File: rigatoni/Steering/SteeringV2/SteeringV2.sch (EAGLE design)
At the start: 19 parts, among them J3 PCB_SCREW_TERM_3, J4 PCB_SCREW_TERM_3, J5 PCB_SCREW_TERM_8, J6 PCB_SCREW_TERM_8, J7 PCB_SCREW_TERM_3, Q1 STT4P3LLH6, U1 SN74ALVC164245DGGR, U2 NUCLEO-H743ZI-HEADER, U3 TPSM84205EAB

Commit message: Commit Internal Design Review
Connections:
- removed net N$7: D2.A, F2.2
- net +5V: now also U2G$3.+5V_CN8; no longer D2.C
- net N$1: now also Q1.D; no longer D1.A, F1.2
- net N$6: now also F1.2; no longer D1.C, Q1.D
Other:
- moved on the sheet: D1, D2
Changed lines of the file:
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@@
 <part name="SUPPLY27" library="RoboJackets-Supplies" deviceset="+3.3V" device=""/>
 <part name="SUPPLY28" library="RoboJackets-Supplies" deviceset="+5V" device=""/>
+<part name="SUPPLY25" library="RoboJackets-Supplies" deviceset="+5V" device=""/>
 </parts>
 <sheets>
@@
 <attribute name="VALUE" x="-29.464" y="84.709" size="1.778" layer="96"/>
 </instance>
-<instance part="D1" gate="G$1" x="-124.46" y="93.98" smashed="yes" rot="R90">
-<attribute name="NAME" x="-119.888" y="90.551" size="1.778" layer="95" font="vector" rot="R180"/>
-<attribute name="VALUE" x="-119.888" y="95.885" size="1.778" layer="96" font="vector" rot="R180" align="top-left"/>
-</instance>
-<instance part="D2" gate="G$1" x="0" y="93.98" smashed="yes" rot="R90">
-<attribute name="NAME" x="4.572" y="90.551" size="1.778" layer="95" font="vector" rot="R180"/>
-<attribute name="VALUE" x="4.572" y="95.885" size="1.778" layer="96" font="vector" rot="R180" align="top-left"/>
+<instance part="D1" gate="G$1" x="-124.46" y="88.9" smashed="yes">
+<attribute name="NAME" x="-127.889" y="84.328" size="1.778" layer="95" font="vector" rot="R90"/>
+<attribute name="VALUE" x="-122.555" y="84.328" size="1.778" layer="96" font="vector" rot="R90" align="top-left"/>
+</instance>
+<instance part="D2" gate="G$1" x="0" y="88.9" smashed="yes">
+<attribute name="NAME" x="-3.429" y="84.328" size="1.778" layer="95" font="vector" rot="R90"/>
+<attribute name="VALUE" x="1.905" y="84.328" size="1.778" layer="96" font="vector" rot="R90" align="top-left"/>
 </instance>
 <instance part="SUPPLY20" gate="P" x="81.28" y="15.24" smashed="yes" rot="R270">
@@
 <instance part="SUPPLY28" gate="G$1" x="106.68" y="129.54" smashed="yes" rot="R270">
 <attribute name="VALUE" x="109.855" y="131.445" size="1.778" layer="96" rot="R270"/>
+</instance>
+<instance part="SUPPLY25" gate="G$1" x="81.28" y="20.32" smashed="yes" rot="R270">
+<attribute name="VALUE" x="84.455" y="22.225" size="1.778" layer="96"/>
 </instance>
 </instances>
@@
 </segment>
 </net>
-<net name="N$1" class="0">
-<segment>
-<pinref part="F1" gate="G$1" pin="2"/>
-<pinref part="D1" gate="G$1" pin="A"/>
-<wire x1="-132.08" y1="93.98" x2="-127" y2="93.98" width="0.1524" layer="91"/>
-</segment>
-</net>
 <net name="N$2" class="0">
 <segment>
@@
 <pinref part="C1" gate="G$1" pin="1"/>
 <wire x1="10.16" y1="93.98" x2="10.16" y2="91.44" width="0.1524" layer="91"/>
-<pinref part="D2" gate="G$1" pin="C"/>
 <wire x1="5.08" y1="93.98" x2="10.16" y2="93.98" width="0.1524" layer="91"/>
 <junction x="10.16" y="93.98"/>
@@
 <junction x="104.14" y="129.54"/>
 </segment>
+<segment>
+<pinref part="U2" gate="G$3" pin="+5V_CN8"/>
+<pinref part="SUPPLY25" gate="G$1" pin="+5V"/>
+<wire x1="63.5" y1="20.32" x2="78.74" y2="20.32" width="0.1524" layer="91"/>
+</segment>
 </net>
 <net name="N$4" class="0">
@@
 <wire x1="-161.29" y1="93.98" x2="-161.29" y2="95.25" width="0.1524" layer="91"/>
 <pinref part="F1" gate="G$1" pin="1"/>
-</segment>
-</net>
-<net name="N$5" class="0">
-<segment>
-<wire x1="-30.48" y1="88.9" x2="-35.56" y2="88.9" width="0.1524" layer="91"/>
-</segment>
-</net>
-<net name="N$6" class="0">
-<segment>
-<pinref part="D1" gate="G$1" pin="C"/>
-<pinref part="Q1" gate="A" pin="D"/>
-<wire x1="-119.38" y1="93.98" x2="-111.76" y2="93.98" width="0.1524" layer="91"/>
-</segment>
-</net>
-<net name="N$7" class="0">
-<segment>
-<pinref part="F2" gate="G$1" pin="2"/>
-<pinref part="D2" gate="G$1" pin="A"/>
-<wire x1="-5.08" y1="93.98" x2="-2.54" y2="93.98" width="0.1524" layer="91"/>
 </segment>
 </net>
@@
 </segment>
 </net>
+<net name="N$1" class="0">
+<segment>
+<pinref part="Q1" gate="A" pin="D"/>
+<wire x1="-116.84" y1="93.98" x2="-111.76" y2="93.98" width="0.1524" layer="91"/>
+</segment>
+</net>
+<net name="N$6" class="0">
+<segment>
+<pinref part="F1" gate="G$1" pin="2"/>
+<wire x1="-132.08" y1="93.98" x2="-127" y2="93.98" width="0.1524" layer="91"/>
+</segment>
+</net>

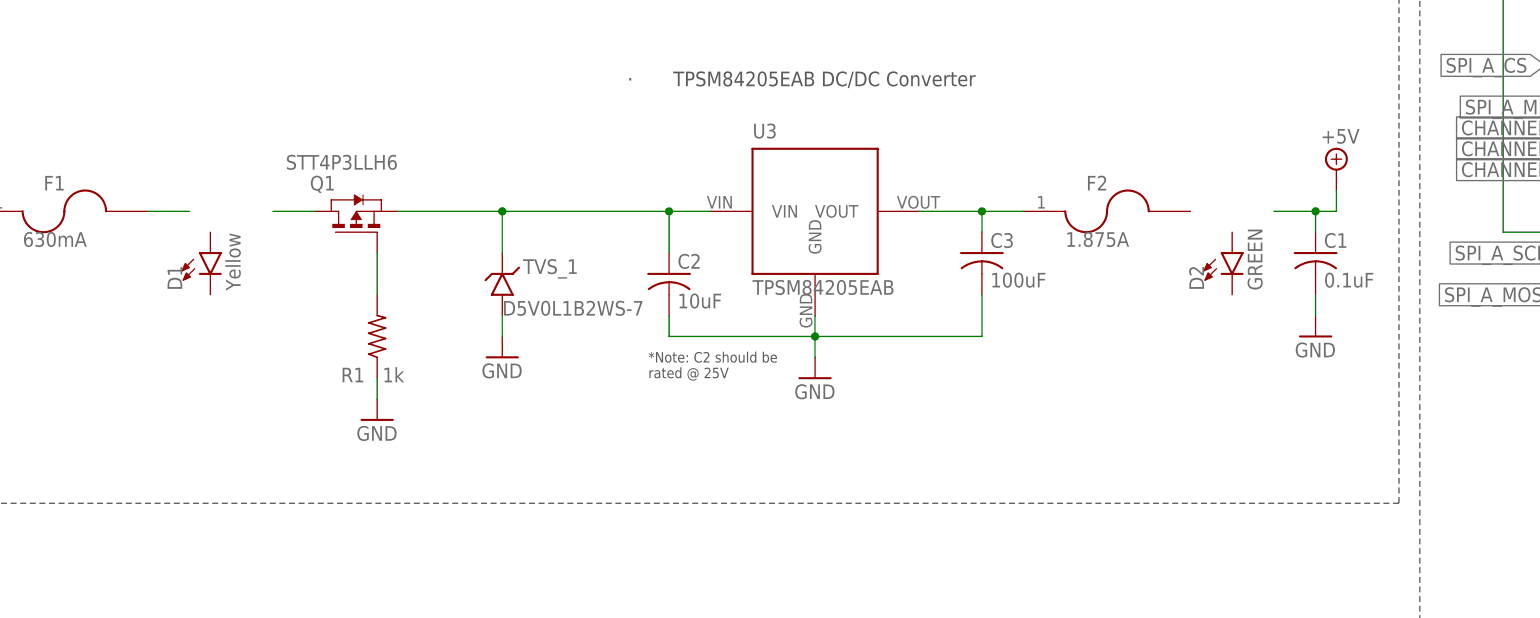
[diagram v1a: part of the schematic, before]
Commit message: Updated Common Power Circuitry
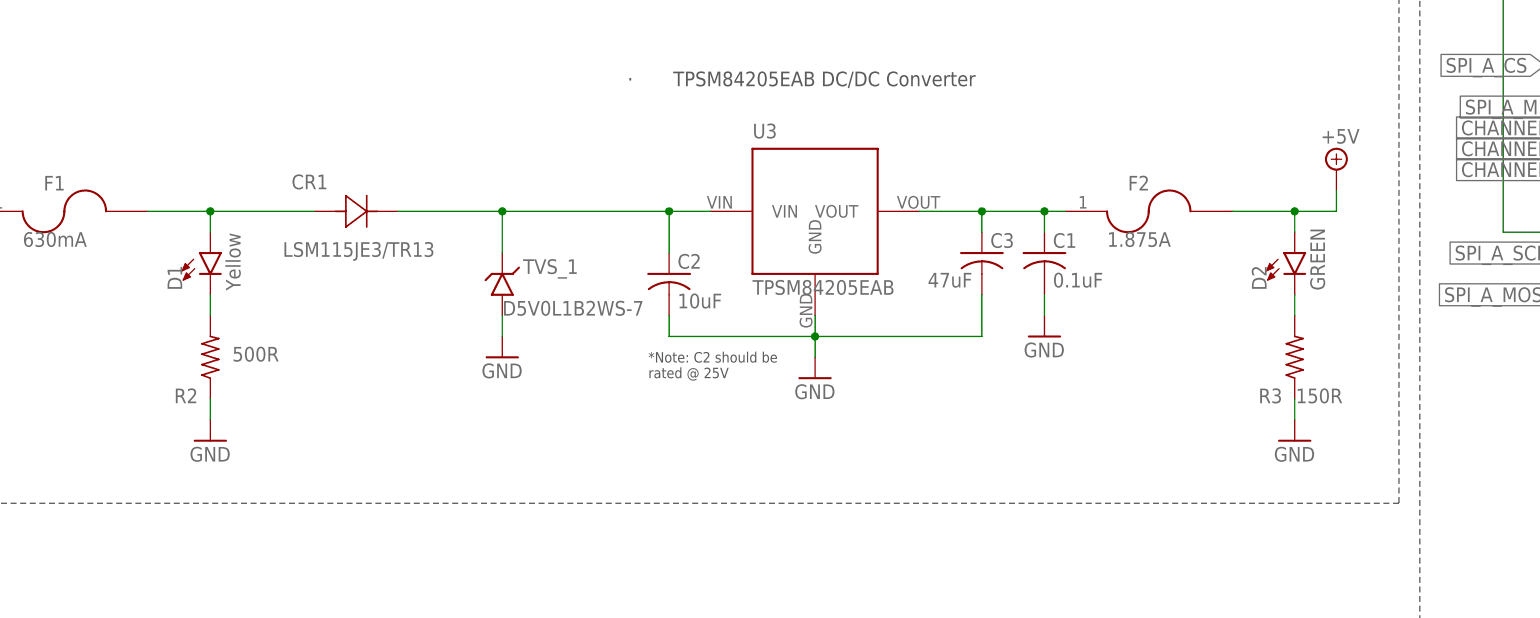
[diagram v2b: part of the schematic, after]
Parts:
- removed Q1: STT4P3LLH6, RoboJackets-Discrete:STT4P3LLH6
- removed R1: 1k, rcl:R-US_R0603
- added CR1: LSM115JE3/TR13, RoboRacing_STM:LSM115JE3/TR13
- added R2: 500R, rcl:R-US_R0603
- added R3: 150R, rcl:R-US_R0603
- C3: value 100uF -> 47uF
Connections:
- removed net N$2: Q1.G, R1.2
- new net N$5: D1.C, R2.2
- net +5V: now also D2.A, F2.2; no longer C1.1
- net 5V_MAIN: now also C1.1
- net GND: now also R2.1, R3.1; no longer R1.1
- net N$1: now also CR1.2, D1.A, F1.2; no longer Q1.D
- net N$3: now also CR1.1; no longer Q1.S
- net N$6: now also D2.C, R3.2; no longer F1.2
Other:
- moved on the sheet: C1, D2, F2

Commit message: Steering Schematic Updated After Internal Design Review
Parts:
- removed J5, J6: PCB_SCREW_TERM_8, RoboJackets-Connectors:PCB_SCREW_TERM_8
- added J2: B10B-XH-A(LF)(SN), RoboRacing_STM:B10B-XH-A(LF)(SN)
- R3: value 150R -> 147R
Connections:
- new net CHANNEL_A_ENC: J2.8, U1.1B5
- new net CHANNEL_B_ENC: J2.7, U1.1B3
- new net CHANNEL_Z_ENC: J2.9, U1.1B7
- new net SPI_A_CS_ENC: J2.1, U1.2B3
- net +5V: now also J2.5; no longer J5.6
- net CHANNEL_A: no longer J6.2, U1.1B5
- net CHANNEL_B: no longer J5.8, U1.1B3
- net CHANNEL_Z: no longer J6.4, U1.1B7
- net GND: now also J2.3, U1.1A1, U1.1A4, U1.1A6, U1.1A8, U1.1B1, U1.1B4, U1.1B6, U1.1B8, U1.2A4, U1.2A5, U1.2A6, U1.2A7, U1.2A8, U1.2B4, U1.2B5, U1.2B6, U1.2B7, U1.2B8; no longer J5.4
- net SPI_A_CS: now also U1.2A3; no longer J5.2, U1.1A1, U1.1B1
- net SPI_A_MISO: now also J2.2; no longer J5.3
- net SPI_A_MOSI: now also J2.6; no longer J5.7
- net SPI_A_SCK: now also J2.4; no longer J5.5

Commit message: Finished Steering V2 Board Layout
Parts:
- removed C1: 0.1uF, rcl:C-US025-024X044
- removed C2: 10uF, rcl:C-US025-024X044
- removed C3: 47uF, rcl:C-US025-024X044
- added C4: 0.1uF, rcl:C-USC0805
- added C5: 47uF, rcl:C-USC0805
- added C6: 10uF, rcl:C-USC0805
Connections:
- net 5V_MAIN: now also C4.1, C5.1; no longer C1.1, C3.1
- net GND: now also C4.2, C5.2, C6.2; no longer C1.2, C2.2, C3.2
- net N$3: now also C6.1; no longer C2.1
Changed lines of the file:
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@@
 <part name="U3" library="RoboRacing_STM" deviceset="TPSM84205EAB" device=""/>
 <part name="SUPPLY6" library="RoboJackets-Supplies" deviceset="GND" device=""/>
-<part name="C2" library="rcl" library_urn="urn:adsk.eagle:library:334" deviceset="C-US" device="025-024X044" package3d_urn="urn:adsk.eagle:package:23630/1" value="10uF"/>
 <part name="F2" library="RoboJackets-Fuses" deviceset="SMD_FUSE" device="0603" value="1.875A"/>
 <part name="SUPPLY9" library="RoboJackets-Supplies" deviceset="GND" device=""/>
@@
 <part name="SUPPLY1" library="RoboJackets-Supplies" deviceset="+5V" device=""/>
 <part name="SUPPLY19" library="RoboJackets-Supplies" deviceset="+5V" device=""/>
-<part name="C1" library="rcl" library_urn="urn:adsk.eagle:library:334" deviceset="C-US" device="025-024X044" package3d_urn="urn:adsk.eagle:package:23630/1" value="0.1uF"/>
 <part name="SUPPLY3" library="RoboJackets-Supplies" deviceset="GND" device=""/>
-<part name="C3" library="rcl" library_urn="urn:adsk.eagle:library:334" deviceset="C-US" device="025-024X044" package3d_urn="urn:adsk.eagle:package:23630/1" value="47uF"/>
 <part name="D1" library="RoboJackets-LEDs" deviceset="LED-YELLOW" device="0603" value="Yellow"/>
 <part name="D2" library="RoboJackets-LEDs" deviceset="LED-GREEN" device="1206" value="GREEN"/>
@@
 <part name="SUPPLY34" library="RoboJackets-Supplies" deviceset="GND" device=""/>
 <part name="SUPPLY35" library="RoboJackets-Supplies" deviceset="GND" device=""/>
+<part name="C4" library="rcl" library_urn="urn:adsk.eagle:library:334" deviceset="C-US" device="C0805" package3d_urn="urn:adsk.eagle:package:23617/2" value="0.1uF"/>
+<part name="C5" library="rcl" library_urn="urn:adsk.eagle:library:334" deviceset="C-US" device="C0805" package3d_urn="urn:adsk.eagle:package:23617/2" value="47uF"/>
+<part name="C6" library="rcl" library_urn="urn:adsk.eagle:library:334" deviceset="C-US" device="C0805" package3d_urn="urn:adsk.eagle:package:23617/2" value="10uF"/>
 </parts>
 <sheets>
@@
 <attribute name="VALUE" x="-53.34" y="71.12" size="1.778" layer="96"/>
 </instance>
-<instance part="C2" gate="G$1" x="-68.58" y="86.36" smashed="yes">
-<attribute name="NAME" x="-67.564" y="86.995" size="1.778" layer="95"/>
-<attribute name="VALUE" x="-67.564" y="82.169" size="1.778" layer="96"/>
-</instance>
 <instance part="F2" gate="G$1" x="-10.16" y="93.98" smashed="yes">
 <attribute name="NAME" x="-12.7" y="96.52" size="1.778" layer="95"/>
@@
 <attribute name="VALUE" x="-24.765" y="31.115" size="1.778" layer="96"/>
 </instance>
-<instance part="C1" gate="G$1" x="-22.86" y="88.9" smashed="yes">
-<attribute name="NAME" x="-21.844" y="89.535" size="1.778" layer="95"/>
-<attribute name="VALUE" x="-21.844" y="84.709" size="1.778" layer="96"/>
-</instance>
 <instance part="SUPPLY3" gate="G$1" x="-22.86" y="78.74" smashed="yes">
 <attribute name="VALUE" x="-25.4" y="76.2" size="1.778" layer="96"/>
-</instance>
-<instance part="C3" gate="G$1" x="-30.48" y="88.9" smashed="yes">
-<attribute name="NAME" x="-29.464" y="89.535" size="1.778" layer="95"/>
-<attribute name="VALUE" x="-37.084" y="84.709" size="1.778" layer="96"/>
 </instance>
 <instance part="D1" gate="G$1" x="-124.46" y="88.9" smashed="yes">
@@
 <instance part="SUPPLY35" gate="G$1" x="104.14" y="96.52" smashed="yes" rot="R90">
 <attribute name="VALUE" x="109.22" y="96.52" size="1.016" layer="96" rot="R180"/>
+</instance>
+<instance part="C4" gate="G$1" x="-22.86" y="88.9" smashed="yes">
+<attribute name="NAME" x="-21.844" y="89.535" size="1.778" layer="95"/>
+<attribute name="VALUE" x="-21.844" y="84.709" size="1.778" layer="96"/>
+</instance>
+<instance part="C5" gate="G$1" x="-30.48" y="88.9" smashed="yes">
+<attribute name="NAME" x="-29.464" y="89.535" size="1.778" layer="95"/>
+<attribute name="VALUE" x="-29.464" y="84.709" size="1.778" layer="96"/>
+</instance>
+<instance part="C6" gate="G$1" x="-68.58" y="86.36" smashed="yes">
+<attribute name="NAME" x="-67.564" y="86.995" size="1.778" layer="95"/>
+<attribute name="VALUE" x="-67.564" y="82.169" size="1.778" layer="96"/>
 </instance>
 </instances>
@@
 <pinref part="SUPPLY6" gate="G$1" pin="GND"/>
 <wire x1="-50.8" y1="81.28" x2="-50.8" y2="78.74" width="0.1524" layer="91"/>
-<pinref part="C2" gate="G$1" pin="2"/>
 <wire x1="-50.8" y1="78.74" x2="-50.8" y2="76.2" width="0.1524" layer="91"/>
-<wire x1="-68.58" y1="81.28" x2="-68.58" y2="78.74" width="0.1524" layer="91"/>
 <wire x1="-68.58" y1="78.74" x2="-50.8" y2="78.74" width="0.1524" layer="91"/>
 <junction x="-50.8" y="78.74"/>
 <wire x1="-30.48" y1="78.74" x2="-50.8" y2="78.74" width="0.1524" layer="91"/>
-<pinref part="C3" gate="G$1" pin="2"/>
+<pinref part="C6" gate="G$1" pin="2"/>
+<wire x1="-68.58" y1="81.28" x2="-68.58" y2="78.74" width="0.1524" layer="91"/>
+<pinref part="C5" gate="G$1" pin="2"/>
 <wire x1="-30.48" y1="83.82" x2="-30.48" y2="78.74" width="0.1524" layer="91"/>
 </segment>
@@
 <pinref part="SUPPLY18" gate="G$1" pin="GND"/>
 <wire x1="-101.6" y1="-116.84" x2="-101.6" y2="-119.38" width="0.1524" layer="91"/>
-</segment>
-<segment>
-<pinref part="C1" gate="G$1" pin="2"/>
-<pinref part="SUPPLY3" gate="G$1" pin="GND"/>
-<wire x1="-22.86" y1="83.82" x2="-22.86" y2="81.28" width="0.1524" layer="91"/>
 </segment>
 <segment>
@@
 <wire x1="99.06" y1="96.52" x2="101.6" y2="96.52" width="0.1524" layer="91"/>
 </segment>
+<segment>
+<pinref part="C4" gate="G$1" pin="2"/>
+<pinref part="SUPPLY3" gate="G$1" pin="GND"/>
+<wire x1="-22.86" y1="83.82" x2="-22.86" y2="81.28" width="0.1524" layer="91"/>
+</segment>
 </net>
 <net name="N$3" class="0">
@@
 <wire x1="-88.9" y1="93.98" x2="-68.58" y2="93.98" width="0.1524" layer="91"/>
 <pinref part="U3" gate="G$1" pin="VIN"/>
-<pinref part="C2" gate="G$1" pin="1"/>
+<pinref part="CR1" gate="A" pin="1"/>
 <wire x1="-68.58" y1="93.98" x2="-63.5" y2="93.98" width="0.1524" layer="91"/>
+<wire x1="-101.6" y1="93.98" x2="-88.9" y2="93.98" width="0.1524" layer="91"/>
+<junction x="-88.9" y="93.98"/>
+<pinref part="C6" gate="G$1" pin="1"/>
 <wire x1="-68.58" y1="88.9" x2="-68.58" y2="93.98" width="0.1524" layer="91"/>
 <junction x="-68.58" y="93.98"/>
-<pinref part="CR1" gate="A" pin="1"/>
-<wire x1="-101.6" y1="93.98" x2="-88.9" y2="93.98" width="0.1524" layer="91"/>
-<junction x="-88.9" y="93.98"/>
 </segment>
 </net>
 <net name="5V_MAIN" class="0">
 <segment>
+<pinref part="C4" gate="G$1" pin="1"/>
+<wire x1="-22.86" y1="91.44" x2="-22.86" y2="93.98" width="0.1524" layer="91"/>
+<pinref part="C5" gate="G$1" pin="1"/>
+<wire x1="-30.48" y1="91.44" x2="-30.48" y2="93.98" width="0.1524" layer="91"/>
 <pinref part="U3" gate="G$1" pin="VOUT"/>
 <wire x1="-38.1" y1="93.98" x2="-30.48" y2="93.98" width="0.1524" layer="91"/>
+<wire x1="-30.48" y1="93.98" x2="-22.86" y2="93.98" width="0.1524" layer="91"/>
+<junction x="-30.48" y="93.98"/>
 <pinref part="F2" gate="G$1" pin="1"/>
-<pinref part="C3" gate="G$1" pin="1"/>
-<wire x1="-30.48" y1="93.98" x2="-22.86" y2="93.98" width="0.1524" layer="91"/>
 <wire x1="-22.86" y1="93.98" x2="-20.32" y2="93.98" width="0.1524" layer="91"/>
-<wire x1="-30.48" y1="93.98" x2="-30.48" y2="91.44" width="0.1524" layer="91"/>
-<junction x="-30.48" y="93.98"/>
-<pinref part="C1" gate="G$1" pin="1"/>
-<wire x1="-22.86" y1="93.98" x2="-22.86" y2="91.44" width="0.1524" layer="91"/>
 <junction x="-22.86" y="93.98"/>
 </segment>

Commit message: Cleaned up
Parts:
- removed J2: B10B-XH-A(LF)(SN), RoboRacing_STM:B10B-XH-A(LF)(SN)
- removed U1: SN74ALVC164245DGGR, RoboRacing_STM:SN74ALVC164245DGGR
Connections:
- removed net CHANNEL_A: U1.1A5, U2G$3.D49/IO
- removed net CHANNEL_A_ENC: J2.8, U1.1B5
- removed net CHANNEL_B: U1.1A3, U2G$5.D8/IO
- removed net CHANNEL_B_ENC: J2.7, U1.1B3
- removed net CHANNEL_Z: U1.1A7, U2G$3.D50/IO
- removed net CHANNEL_Z_ENC: J2.9, U1.1B7
- removed net SPI_A_CS: U1.2A3, U2G$5.D10/SPI_A_CS/TIM_B_PWM3
- removed net SPI_A_CS_ENC: J2.1, U1.2B3
- removed net SPI_A_MISO: J2.2, U1.1A2, U1.1B2, U2G$5.D12/SPI_A_MISO
- removed net SPI_A_MOSI: J2.6, U1.2A2, U1.2B2, U2G$5.D11/SPI_A_MOSI/TIM_E_PWM1
- removed net SPI_A_SCK: J2.4, U1.2A1, U1.2B1, U2G$5.D13/SPI_A_SCK
- removed net USART_B_RX: J4.1, U2G$4.D52/USART_B_RX
- removed net USART_B_TX: J4.2, U2G$4.D53/USART_B_TX
- new net USART_A_RX: J4.1, U2G$6.D0/USART_A_RX
- new net USART_A_TX: J4.2, U2G$6.D1/USART_A_TX
- net +3.3V: no longer U1.2DIR, U1.VCCA_31, U1.VCCA_42
- net +5V: no longer J2.5, U1.VCCB_18, U1.VCCB_7, U2G$3.VIN_CN8, U2G$5.AREF
- net GND: now also U2G$2.AGND_CN12, U2G$2.GND_CN12, U2G$6.AGND_CN10, U2G$6.GND_CN10; no longer J2.3, U1.1!OE, U1.1A1, U1.1A4, U1.1A6, U1.1A8, U1.1B1, U1.1B4, U1.1B6, U1.1B8, U1.1DIR, U1.2!OE, U1.2A4, U1.2A5, U1.2A6, U1.2A7, U1.2A8, U1.2B4, U1.2B5, U1.2B6, U1.2B7, U1.2B8, U1.GND_10, U1.GND_15, U1.GND_21, U1.GND_28, U1.GND_34, U1.GND_39, U1.GND_4, U1.GND_45
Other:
- note removed: "ABSOLUTE ENCODER CONNECTORS"
